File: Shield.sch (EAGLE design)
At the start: 71 parts

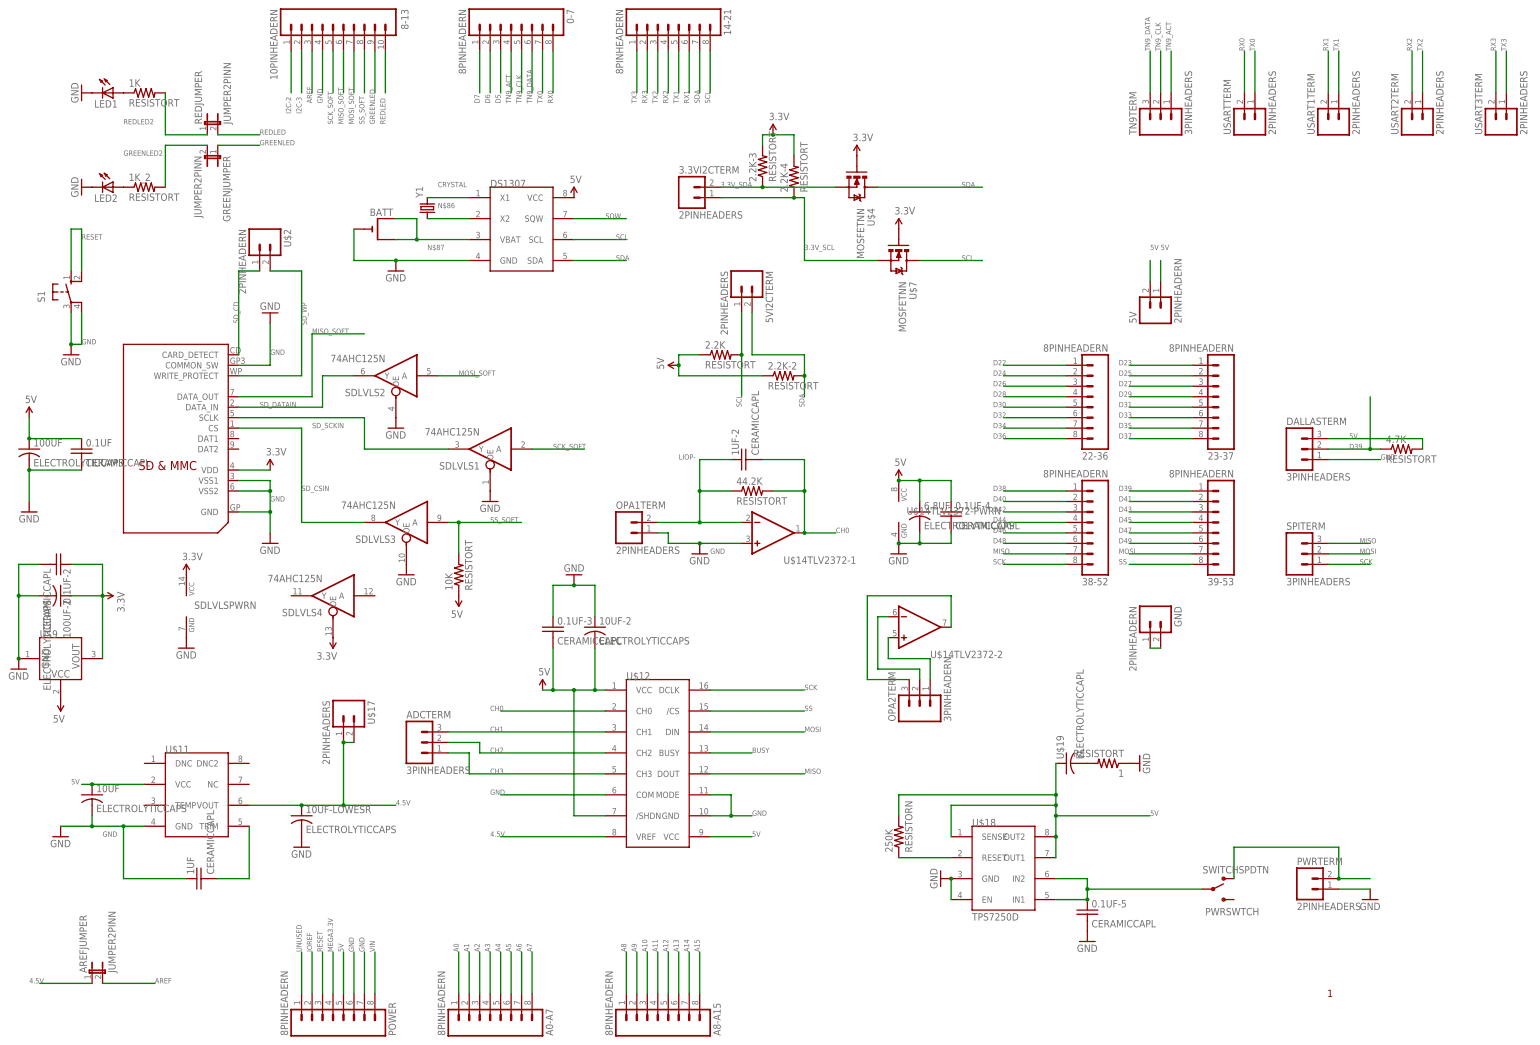
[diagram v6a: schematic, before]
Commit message: All components on board
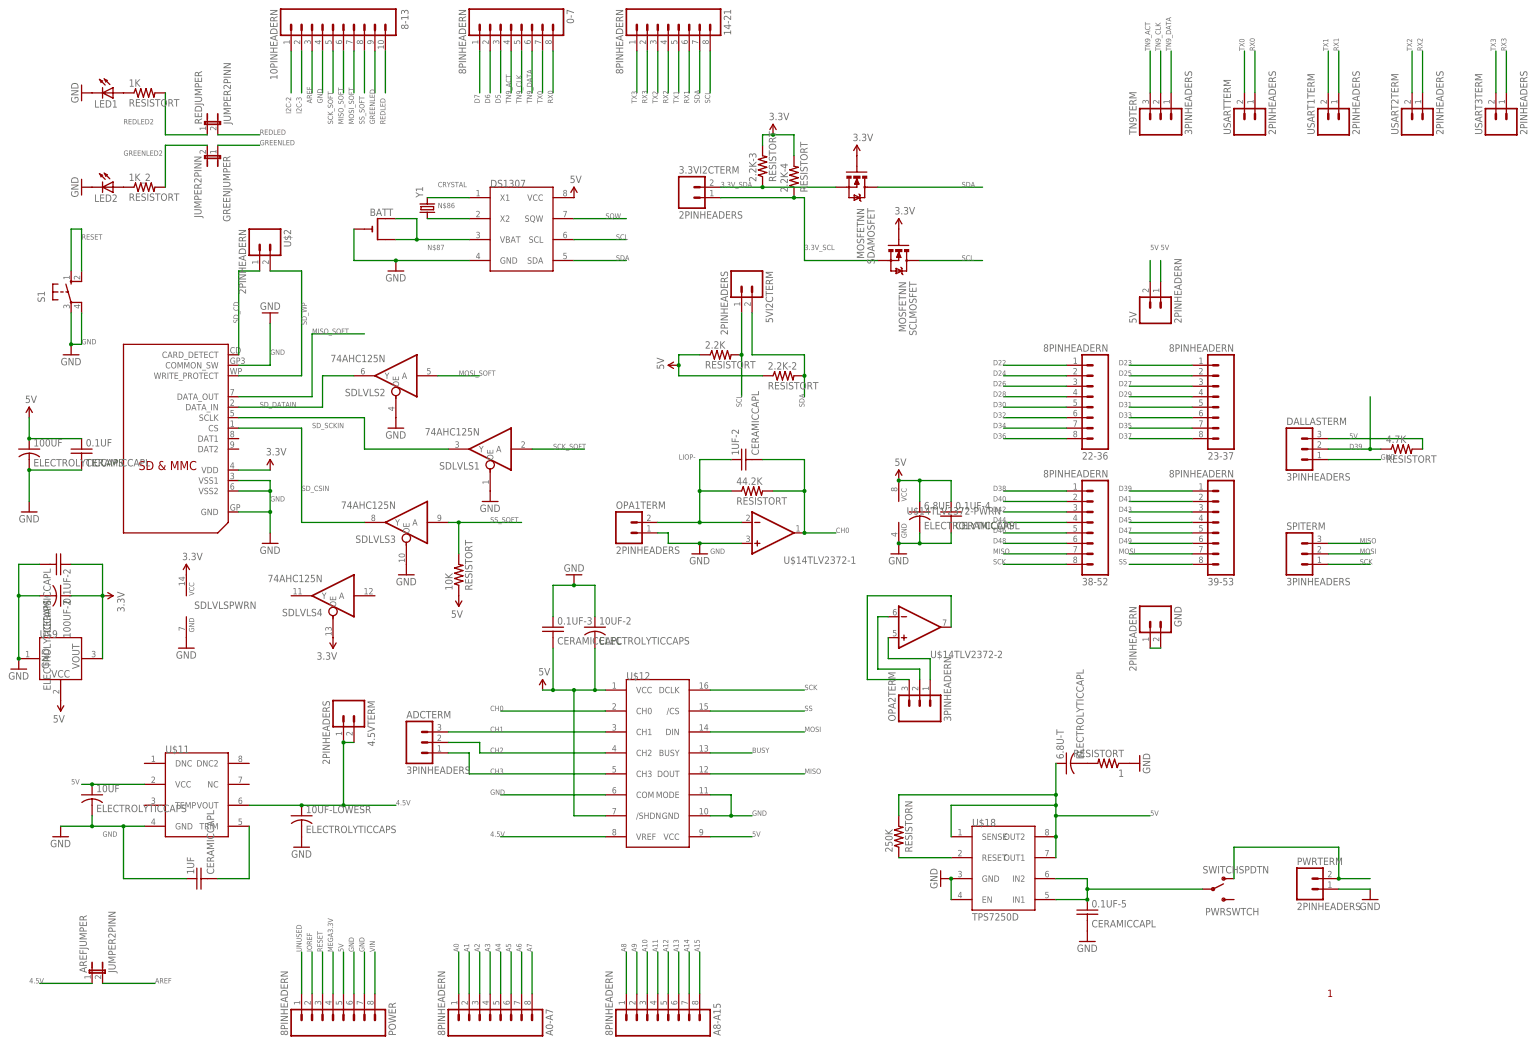
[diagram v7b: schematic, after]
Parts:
- renumbered U$17 to 4.5VTERM, U$19 to 6.8U-T, U$4 to SDAMOSFET, U$7 to SCLMOSFET
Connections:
- net RX0: now also USARTTERM.1; no longer USARTTERM.2
- net RX1: now also USART1TERM.1; no longer USART1TERM.2
- net RX2: now also USART2TERM.1; no longer USART2TERM.2
- net RX3: now also USART3TERM.1; no longer USART3TERM.2
- net TN9_ACT: now also TN9TERM.3; no longer TN9TERM.1
- net TN9_DATA: now also TN9TERM.1; no longer TN9TERM.3
- net TX0: now also USARTTERM.2; no longer USARTTERM.1
- net TX1: now also USART1TERM.2; no longer USART1TERM.1
- net TX2: now also USART2TERM.2; no longer USART2TERM.1
- net TX3: now also USART3TERM.2; no longer USART3TERM.1

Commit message: Started Routing
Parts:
- 0-7, 14-21, 22-36, 23-37, 38-52, 39-53, A0-A7, A8-A15, POWER: value 8PINHEADERN -> 8PHN; device LEMS:8PINHEADERN -> LEMS:8PHN
- 0.1UF, 0.1UF-2, 0.1UF-3, 0.1UF-4, 0.1UF-5, 1UF, 1UF-2: value CERAMICCAPL -> CCL; device LEMS:CERAMICCAPL -> LEMS:CCL
- 1, 10K, 1K, 1K_2, 2.2K, 2.2K-2, 2.2K-3, 2.2K-4: value RESISTORT -> RT; device LEMS:RESISTORT -> LEMS:RT
- 100UF-2, 10UF, 10UF-2, 10UF-LOWESR, 6.8UF: value ELECTROLYTICCAPS -> CES; device LEMS:ELECTROLYTICCAPS -> LEMS:CES
- 250K: value RESISTORN -> RN; device LEMS:RESISTORN -> LEMS:RN
- 3.3VI2CTERM, 4.5VTERM, 5VI2CTERM, OPA1TERM, PWRTERM, USART1TERM, USART2TERM, USART3TERM, USARTTERM: value 2PINHEADERS -> 2PHS; device LEMS:2PINHEADERS -> LEMS:2PHS
- 5V, GND, U$2: value 2PINHEADERN -> 2PHN; device LEMS:2PINHEADERN -> LEMS:2PHN
- 6.8U-T: value ELECTROLYTICCAPL -> CES; device LEMS:ELECTROLYTICCAPL -> LEMS:CES
- 8-13: value 10PINHEADERN -> 10PHN; device LEMS:10PINHEADERN -> LEMS:10PHN
- ADCTERM, DALLASTERM, SPITERM, TN9TERM: value 3PINHEADERS -> 3PHS; device LEMS:3PINHEADERS -> LEMS:3PHS
- AREFJUMPER, GREENJUMPER, REDJUMPER: value JUMPER2PINN -> 2PJN; device LEMS:JUMPER2PINN -> LEMS:2PJN
- OPA2TERM: value 3PINHEADERN -> 3PHN; device LEMS:3PINHEADERN -> LEMS:3PHN
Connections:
- removed net N$87: BATT.+, BATT.+1, DS1307.VBAT
- new net VBAT: BATT.+, DS1307.VBAT
